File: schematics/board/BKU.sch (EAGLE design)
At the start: 60 parts

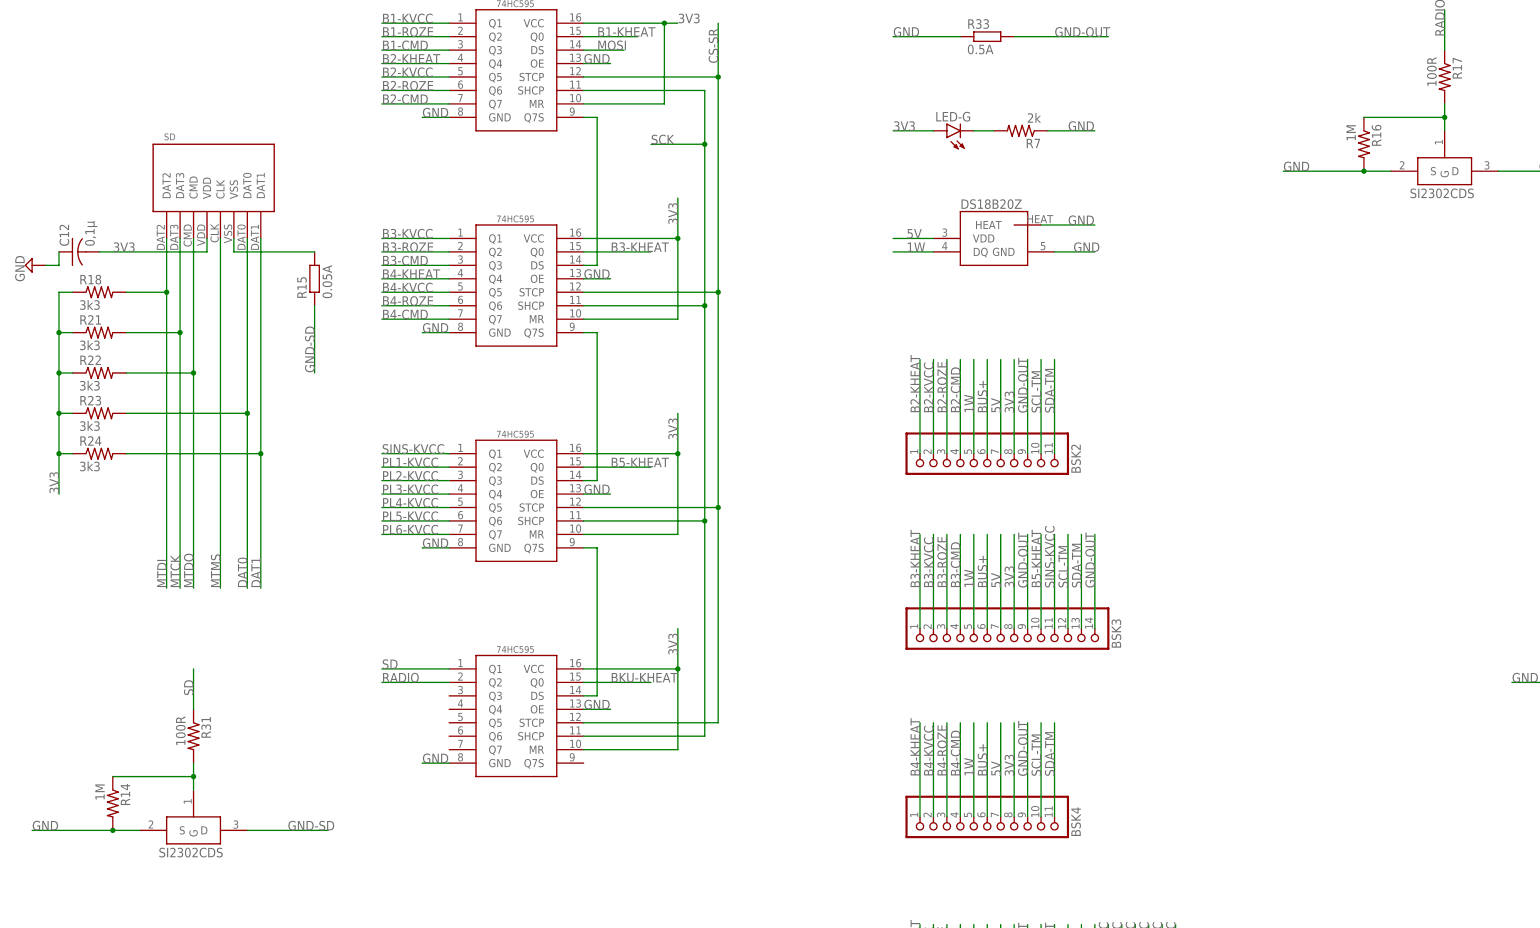
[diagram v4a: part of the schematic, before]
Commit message: На платах БСК устройства по умолчанию подтянуты к питанию
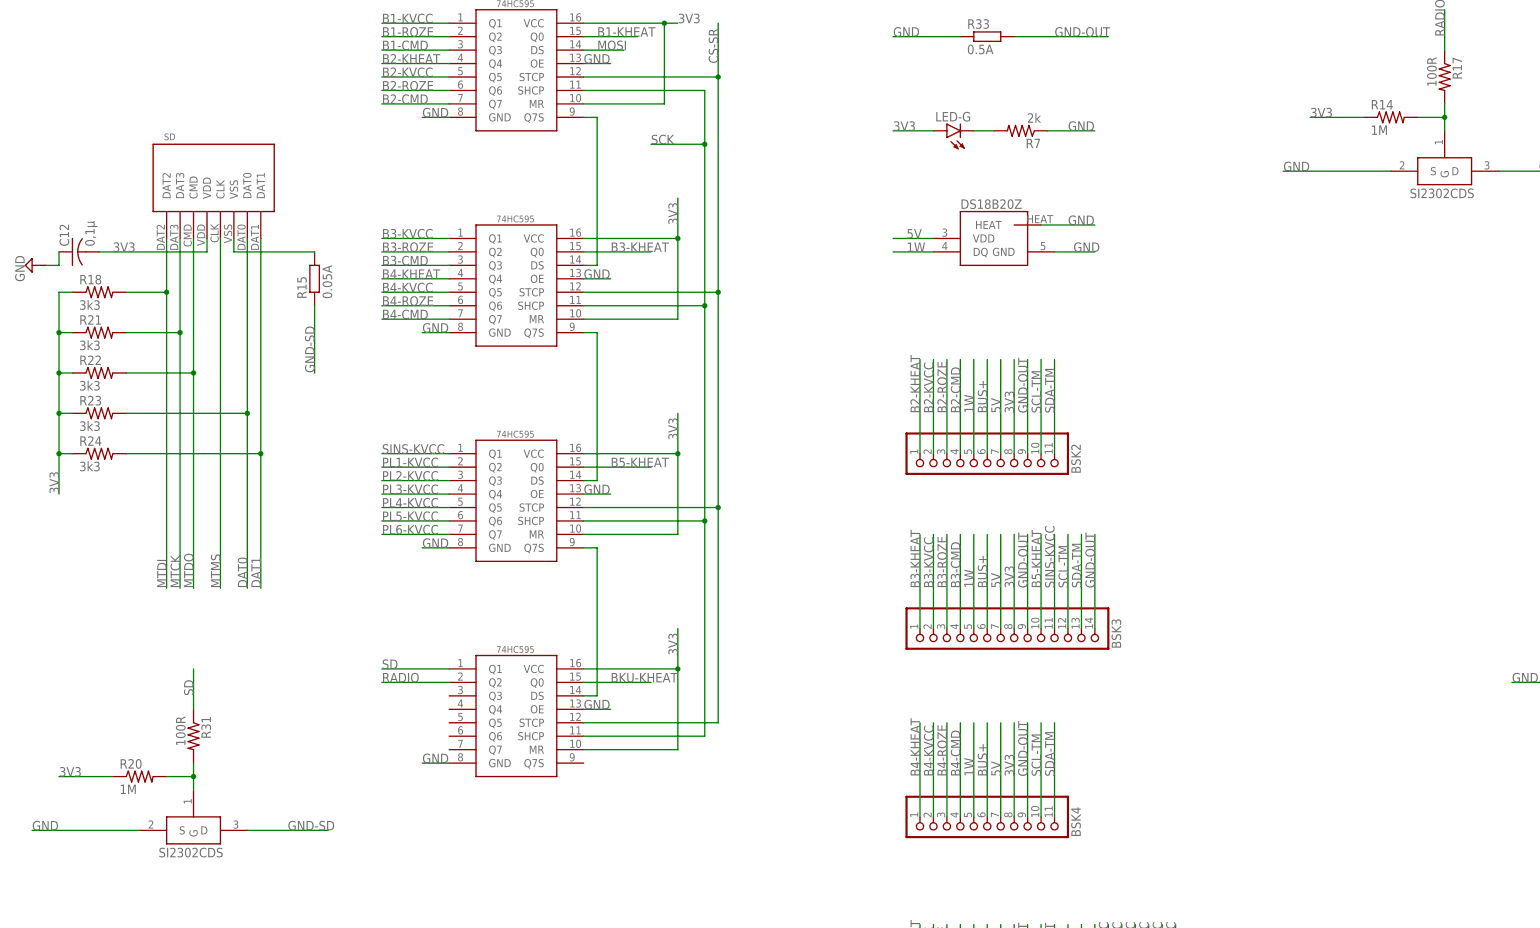
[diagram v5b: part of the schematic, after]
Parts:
- removed R16: 1M, resistor:R-US_R0603
- added R20: 1M, resistor:R-US_R0603
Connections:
- net 3V3: now also R14.1, R20.1
- net GND: no longer R14.2, R16.2
- net N$11: now also R20.2; no longer R14.1
- net N$6: now also R14.2; no longer R16.1
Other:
- moved on the sheet: R14
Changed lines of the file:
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@@
 <part name="LED-G" library="led" library_urn="urn:adsk.eagle:library:259" deviceset="LED" device="CHIPLED_0603" package3d_urn="urn:adsk.eagle:package:15822/2"/>
 <part name="U$3" library="CanCubeSat" deviceset="SI2302CDS" device=""/>
-<part name="R14" library="resistor" deviceset="R-US_" device="R0603" package3d_urn="urn:adsk.eagle:package:23555/3" value="1M"/>
 <part name="R31" library="resistor" deviceset="R-US_" device="R0603" package3d_urn="urn:adsk.eagle:package:23555/3" value="100R"/>
 <part name="R33" library="rcl" library_urn="urn:adsk.eagle:library:334" deviceset="R-EU_" device="R1210" package3d_urn="urn:adsk.eagle:package:23554/2" value="0.5A"/>
 <part name="R15" library="rcl" library_urn="urn:adsk.eagle:library:334" deviceset="R-EU_" device="R1210" package3d_urn="urn:adsk.eagle:package:23554/2" value="0.05A"/>
 <part name="U$4" library="CanCubeSat" deviceset="SI2302CDS" device=""/>
-<part name="R16" library="resistor" deviceset="R-US_" device="R0603" package3d_urn="urn:adsk.eagle:package:23555/3" value="1M"/>
 <part name="R17" library="resistor" deviceset="R-US_" device="R0603" package3d_urn="urn:adsk.eagle:package:23555/3" value="100R"/>
 <part name="R19" library="rcl" library_urn="urn:adsk.eagle:library:334" deviceset="R-EU_" device="R1210" package3d_urn="urn:adsk.eagle:package:23554/2" value="0.5A"/>
+<part name="R20" library="resistor" deviceset="R-US_" device="R0603" package3d_urn="urn:adsk.eagle:package:23555/3" value="1M"/>
+<part name="R14" library="resistor" deviceset="R-US_" device="R0603" package3d_urn="urn:adsk.eagle:package:23555/3" value="1M"/>
 </parts>
 <sheets>
@@
 </instance>
 <instance part="U$3" gate="G$1" x="58.42" y="121.92" smashed="yes"/>
-<instance part="R14" gate="G$1" x="43.18" y="127" smashed="yes" rot="R270">
-<attribute name="NAME" x="44.6786" y="130.81" size="1.778" layer="95" rot="R270"/>
-<attribute name="VALUE" x="39.878" y="130.81" size="1.778" layer="96" rot="R270"/>
-</instance>
 <instance part="R31" gate="G$1" x="58.42" y="139.7" smashed="yes" rot="R270">
 <attribute name="NAME" x="59.9186" y="143.51" size="1.778" layer="95" rot="R270"/>
@@
 </instance>
 <instance part="U$4" gate="G$1" x="294.64" y="246.38" smashed="yes"/>
-<instance part="R16" gate="G$1" x="279.4" y="251.46" smashed="yes" rot="R270">
-<attribute name="NAME" x="280.8986" y="255.27" size="1.778" layer="95" rot="R270"/>
-<attribute name="VALUE" x="276.098" y="255.27" size="1.778" layer="96" rot="R270"/>
-</instance>
 <instance part="R17" gate="G$1" x="294.64" y="264.16" smashed="yes" rot="R270">
 <attribute name="NAME" x="296.1386" y="267.97" size="1.778" layer="95" rot="R270"/>
@@
 <attribute name="NAME" x="372.11" y="217.3986" size="1.778" layer="95"/>
 <attribute name="VALUE" x="372.11" y="212.598" size="1.778" layer="96"/>
+</instance>
+<instance part="R20" gate="G$1" x="48.26" y="132.08" smashed="yes">
+<attribute name="NAME" x="44.45" y="133.5786" size="1.778" layer="95"/>
+<attribute name="VALUE" x="44.45" y="128.778" size="1.778" layer="96"/>
+</instance>
+<instance part="R14" gate="G$1" x="284.48" y="256.54" smashed="yes">
+<attribute name="NAME" x="280.67" y="258.0386" size="1.778" layer="95"/>
+<attribute name="VALUE" x="280.67" y="253.238" size="1.778" layer="96"/>
 </instance>
 </instances>
@@
 <segment>
 <pinref part="U$3" gate="G$1" pin="S"/>
-<wire x1="48.26" y1="121.92" x2="43.18" y2="121.92" width="0.1524" layer="91"/>
 <label x="27.94" y="121.92" size="1.778" layer="95"/>
-<pinref part="R14" gate="G$1" pin="2"/>
-<wire x1="43.18" y1="121.92" x2="27.94" y2="121.92" width="0.1524" layer="91"/>
-<junction x="43.18" y="121.92"/>
+<wire x1="48.26" y1="121.92" x2="27.94" y2="121.92" width="0.1524" layer="91"/>
 </segment>
 <segment>
@@
 <segment>
 <pinref part="U$4" gate="G$1" pin="S"/>
-<wire x1="284.48" y1="246.38" x2="279.4" y2="246.38" width="0.1524" layer="91"/>
 <label x="264.16" y="246.38" size="1.778" layer="95"/>
-<pinref part="R16" gate="G$1" pin="2"/>
-<wire x1="279.4" y1="246.38" x2="264.16" y2="246.38" width="0.1524" layer="91"/>
-<junction x="279.4" y="246.38"/>
+<wire x1="284.48" y1="246.38" x2="264.16" y2="246.38" width="0.1524" layer="91"/>
 </segment>
 <segment>
@@
 <wire x1="198.12" y1="254" x2="190.5" y2="254" width="0.1524" layer="91"/>
 </segment>
+<segment>
+<pinref part="R20" gate="G$1" pin="1"/>
+<wire x1="43.18" y1="132.08" x2="33.02" y2="132.08" width="0.1524" layer="91"/>
+<label x="33.02" y="132.08" size="1.778" layer="95"/>
+</segment>
+<segment>
+<pinref part="R14" gate="G$1" pin="1"/>
+<wire x1="279.4" y1="256.54" x2="269.24" y2="256.54" width="0.1524" layer="91"/>
+<label x="269.24" y="256.54" size="1.778" layer="95"/>
+</segment>
 </net>
 <net name="PL6-KVCC" class="0">
@@
 <pinref part="U$3" gate="G$1" pin="G"/>
 <wire x1="58.42" y1="134.62" x2="58.42" y2="132.08" width="0.1524" layer="91"/>
-<pinref part="R14" gate="G$1" pin="1"/>
+<pinref part="R20" gate="G$1" pin="2"/>
 <wire x1="58.42" y1="132.08" x2="58.42" y2="129.54" width="0.1524" layer="91"/>
-<wire x1="43.18" y1="132.08" x2="58.42" y2="132.08" width="0.1524" layer="91"/>
+<wire x1="53.34" y1="132.08" x2="58.42" y2="132.08" width="0.1524" layer="91"/>
 <junction x="58.42" y="132.08"/>
 </segment>
@@
 <pinref part="U$4" gate="G$1" pin="G"/>
 <wire x1="294.64" y1="259.08" x2="294.64" y2="256.54" width="0.1524" layer="91"/>
-<pinref part="R16" gate="G$1" pin="1"/>
+<pinref part="R14" gate="G$1" pin="2"/>
 <wire x1="294.64" y1="256.54" x2="294.64" y2="254" width="0.1524" layer="91"/>
-<wire x1="279.4" y1="256.54" x2="294.64" y2="256.54" width="0.1524" layer="91"/>
+<wire x1="289.56" y1="256.54" x2="294.64" y2="256.54" width="0.1524" layer="91"/>
 <junction x="294.64" y="256.54"/>
 </segment>

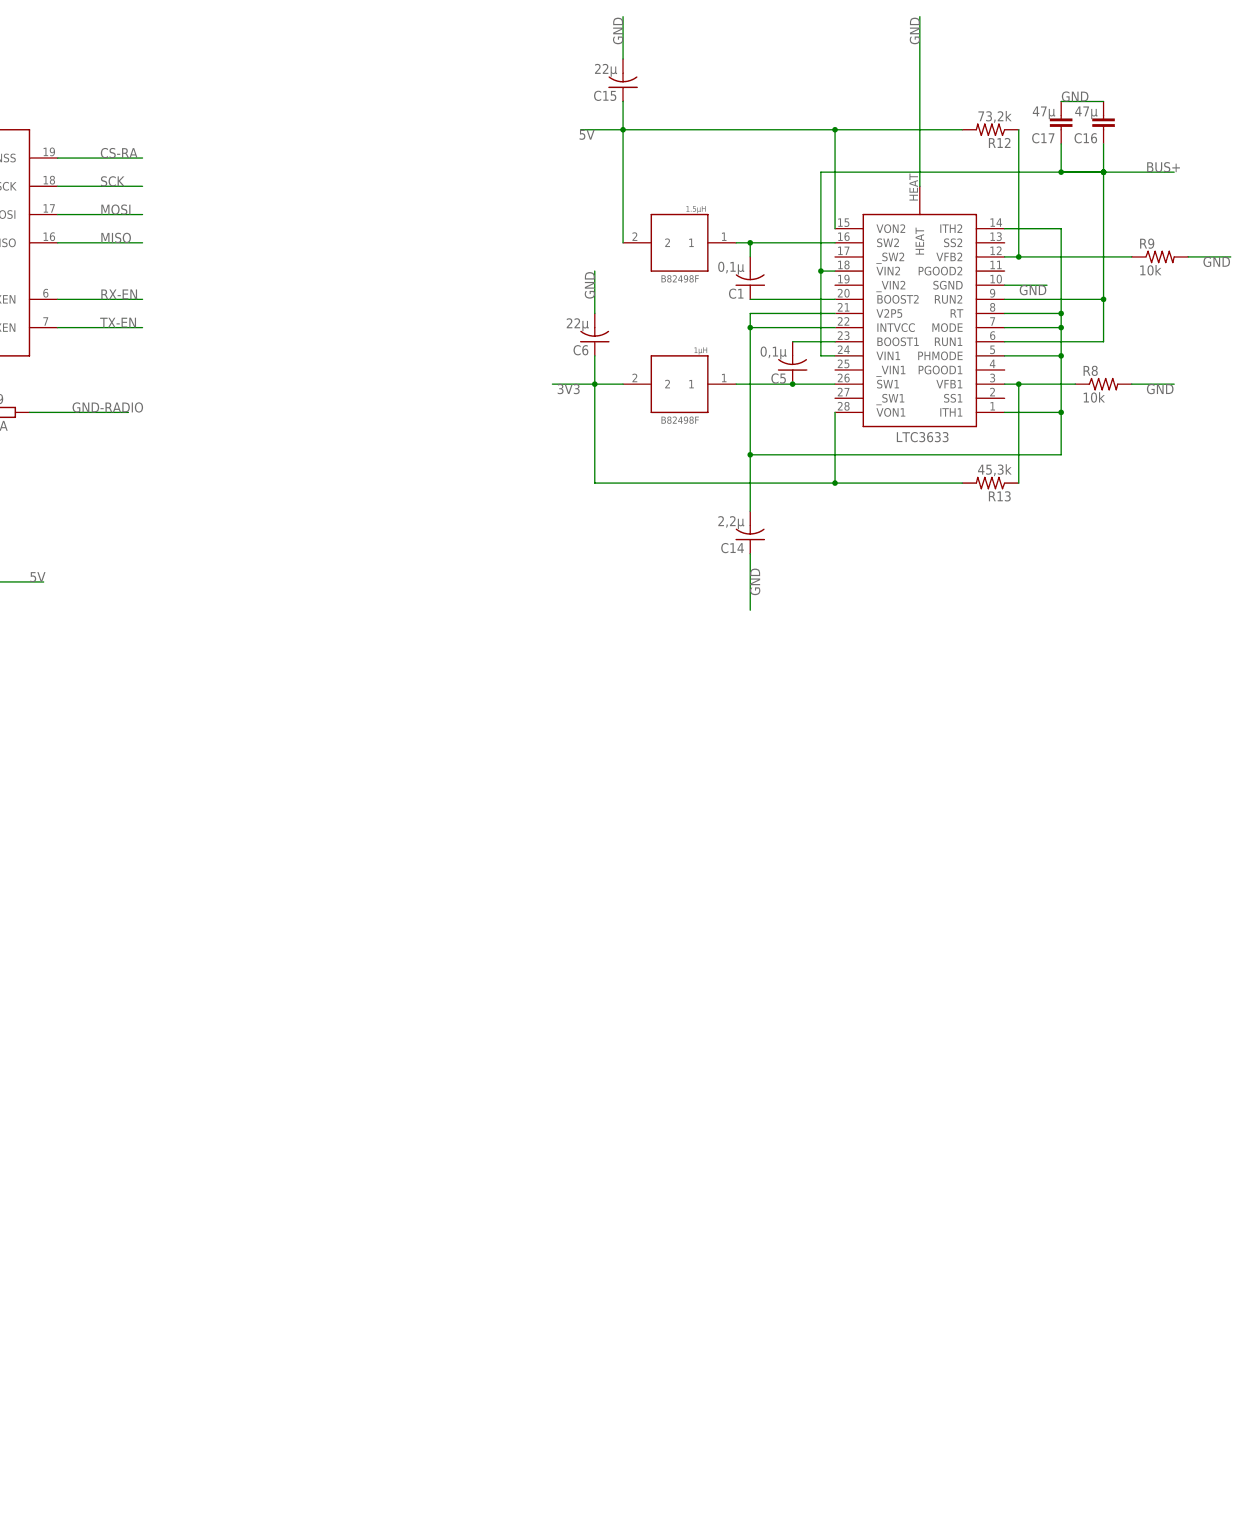
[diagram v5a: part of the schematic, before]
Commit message: Сделана схема БКУ
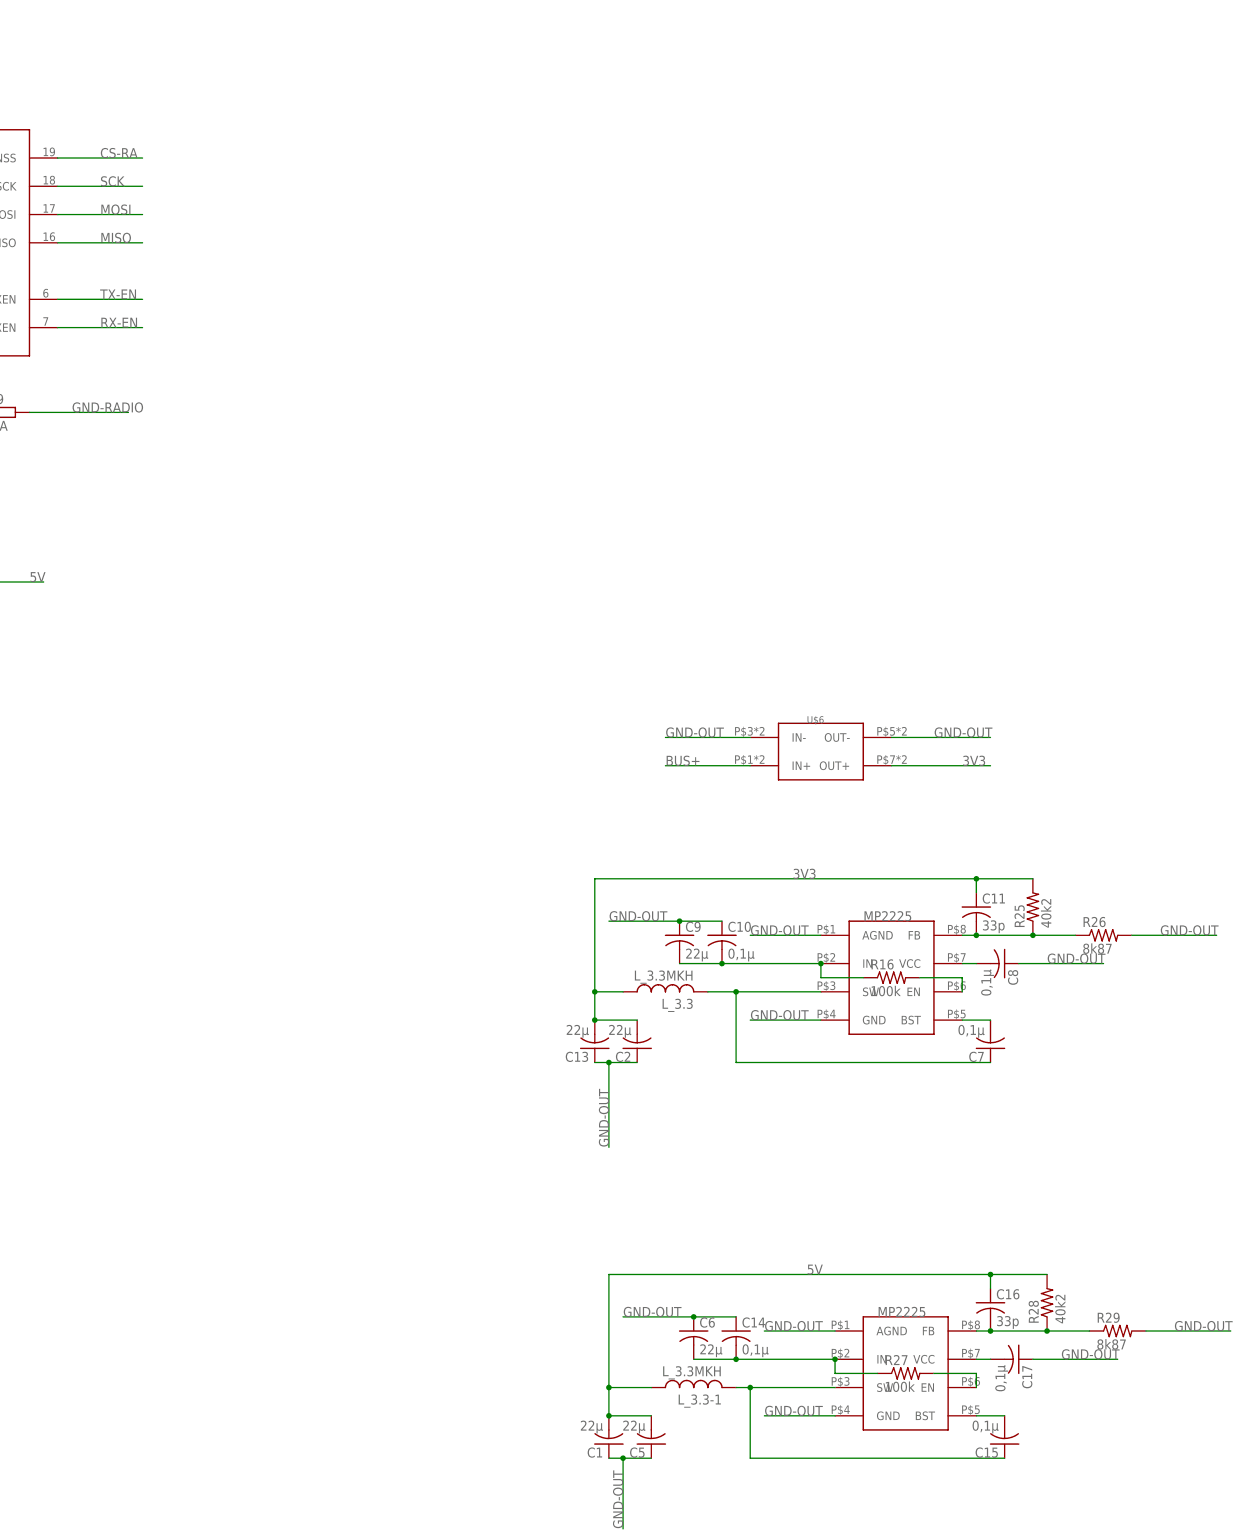
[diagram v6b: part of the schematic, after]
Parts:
- removed R12: 73,2k, resistor:R-US_R0603
- removed R13: 45,3k, resistor:R-US_R0603
- removed R8, R9: 10k, resistor:R-US_R0603
- removed U$10: LTC3633, CanCubeSat:LTC3633
- removed U$11: 1µH, CanCubeSat:B82498F
- removed U$12: B82498F, CanCubeSat:B82498F
- added C10, C7, C8: 0,1µ, rcl:C-USC0603
- added C11: 33p, rcl:C-USC0603
- added C13, C2, C9: 22µ, rcl:C-USC1206
- added L_3.3, L_3.3-1: L_3.3MKH, CanCubeSat:L_3.3MKH_5X5
- added MP2225, MP2225-1: MP2225, CanCubeSat:MP2225
- added R16, R27: 100k, resistor:R-US_R0603
- added R25, R28: 40k2, resistor:R-US_R0603
- added R26, R29: 8k87, resistor:R-US_R0603
- added U$6: MP1584-B, CanCubeSat:MP1584-B
- C1, C5: value 0,1µ -> 22µ; device rcl:C-USC0603 -> rcl:C-USC1206
- C14: value 2,2µ -> 0,1µ
- C15: value 22µ -> 0,1µ; device rcl:C-USC1206 -> rcl:C-USC0603
- C16: value 47µ -> 33p; device rcl:C-EUC1210 -> rcl:C-USC0603
- C17: value 47µ -> 0,1µ; device rcl:C-EUC1210 -> rcl:C-USC0603
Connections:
- removed net N$24: C14.2, U$10.INTVCC, U$10.ITH1, U$10.ITH2, U$10.MODE, U$10.PHMODE, U$10.RT, U$10.V2P5
- removed net N$25: R13.1, R8.1, U$10.VFB1
- removed net N$28: C5.1, U$10.SW1, U$11.1
- removed net N$31: C5.2, U$10.BOOST1
- removed net N$32: C1.1, U$10.BOOST2
- removed net N$33: C1.2, U$10.SW2, U$12.1
- removed net N$39: R12.1, R9.1, U$10.VFB2
- new net N$10: MP2225-1.EN, R27.2
- new net N$12: C17.2, MP2225-1.VCC
- new net N$13: C7.2, MP2225.BST
- new net N$14: C7.1, L_3.3.2, MP2225.SW
- new net N$15: MP2225.EN, R16.2
- new net N$16: C8.2, MP2225.VCC
- new net N$20: C11.2, MP2225.FB, R25.1, R26.1
- new net N$21: C10.2, C9.2, MP2225.IN, R16.1
- new net N$22: C16.2, MP2225-1.FB, R28.1, R29.1
- new net N$7: C14.2, C6.2, MP2225-1.IN, R27.1
- new net N$8: C15.1, L_3.3-1.2, MP2225-1.SW
- new net N$9: C15.2, MP2225-1.BST
- net 3V3: now also C11.1, C13.2, C2.2, L_3.3.1, R25.2, U$6.OUT+; no longer C6.1, R13.2, U$10.VON1, U$11.2
- net 5V: now also C1.2, C16.1, C5.2, L_3.3-1.1, R28.2; no longer C15.1, R12.2, U$10.VON2, U$12.2
- net BUS+: now also U$6.IN+; no longer C16.1, C17.1, U$10.RUN1, U$10.RUN2, U$10.VIN1, U$10.VIN2
- net GND: no longer C14.1, C15.2, C16.2, C17.2, C6.2, R8.2, R9.2, U$10.HEAT, U$10.SGND
- net GND-OUT: now also C1.1, C10.1, C13.1, C14.1, C17.1, C2.1, C5.1, C6.1, C8.1, C9.1, MP2225-1.AGND, MP2225-1.GND, MP2225.AGND, MP2225.GND, R26.2, R29.2, U$6.IN-, U$6.OUT-
- net RX-EN: now also U$1.TXEN; no longer U$1.RXEN
- net TX-EN: now also U$1.RXEN; no longer U$1.TXEN
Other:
- note removed: "1.5µH"
- note removed: "1µH"
- moved on the sheet: C1, C14, C15, C16, C17, C5, C6
